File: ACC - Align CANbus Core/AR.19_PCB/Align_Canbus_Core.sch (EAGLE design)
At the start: 32 parts

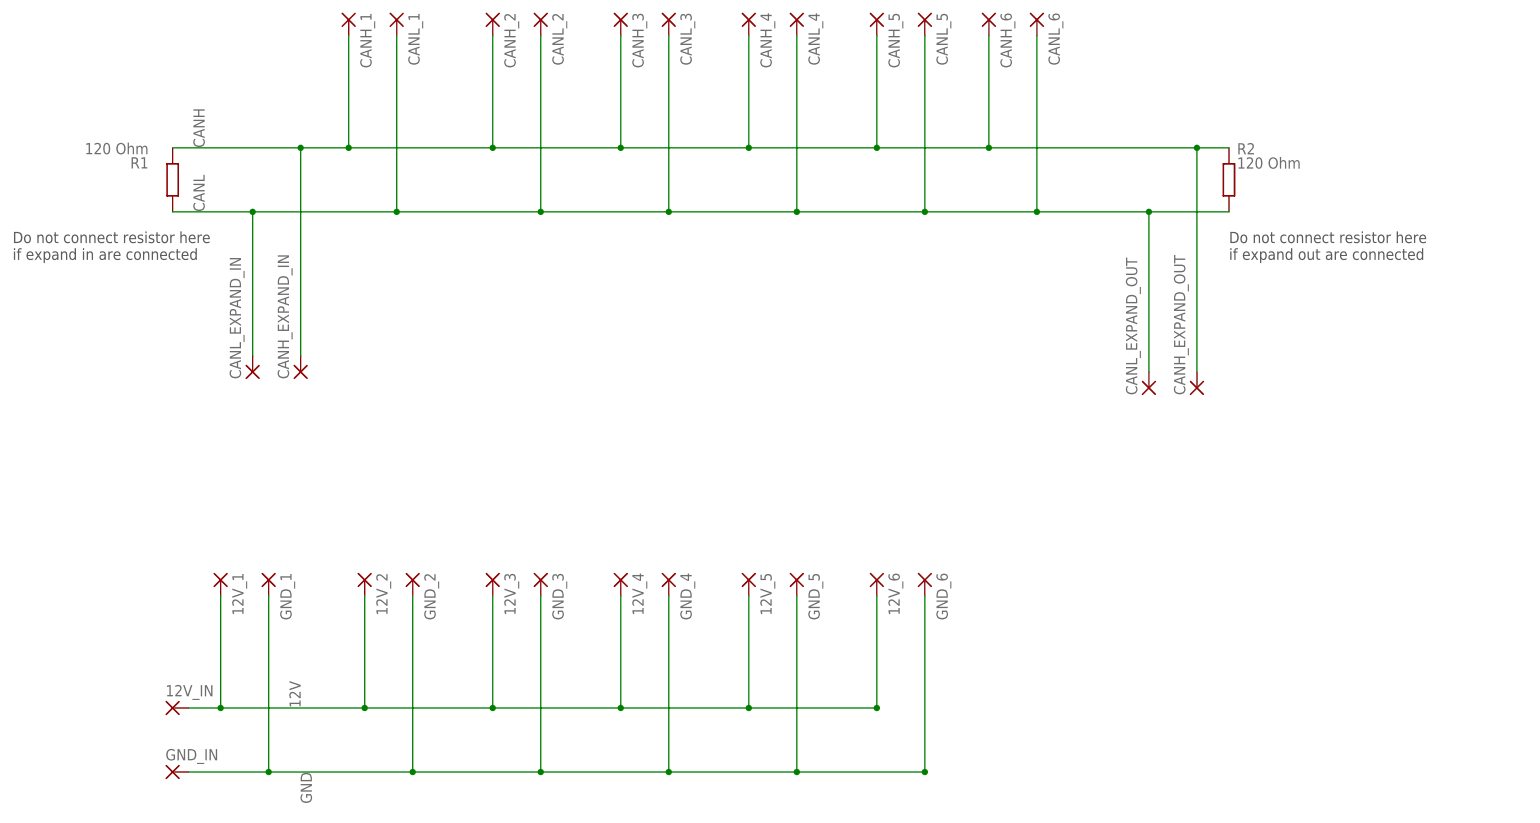
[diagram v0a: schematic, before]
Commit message: CANbus Core: Input and output expansion added
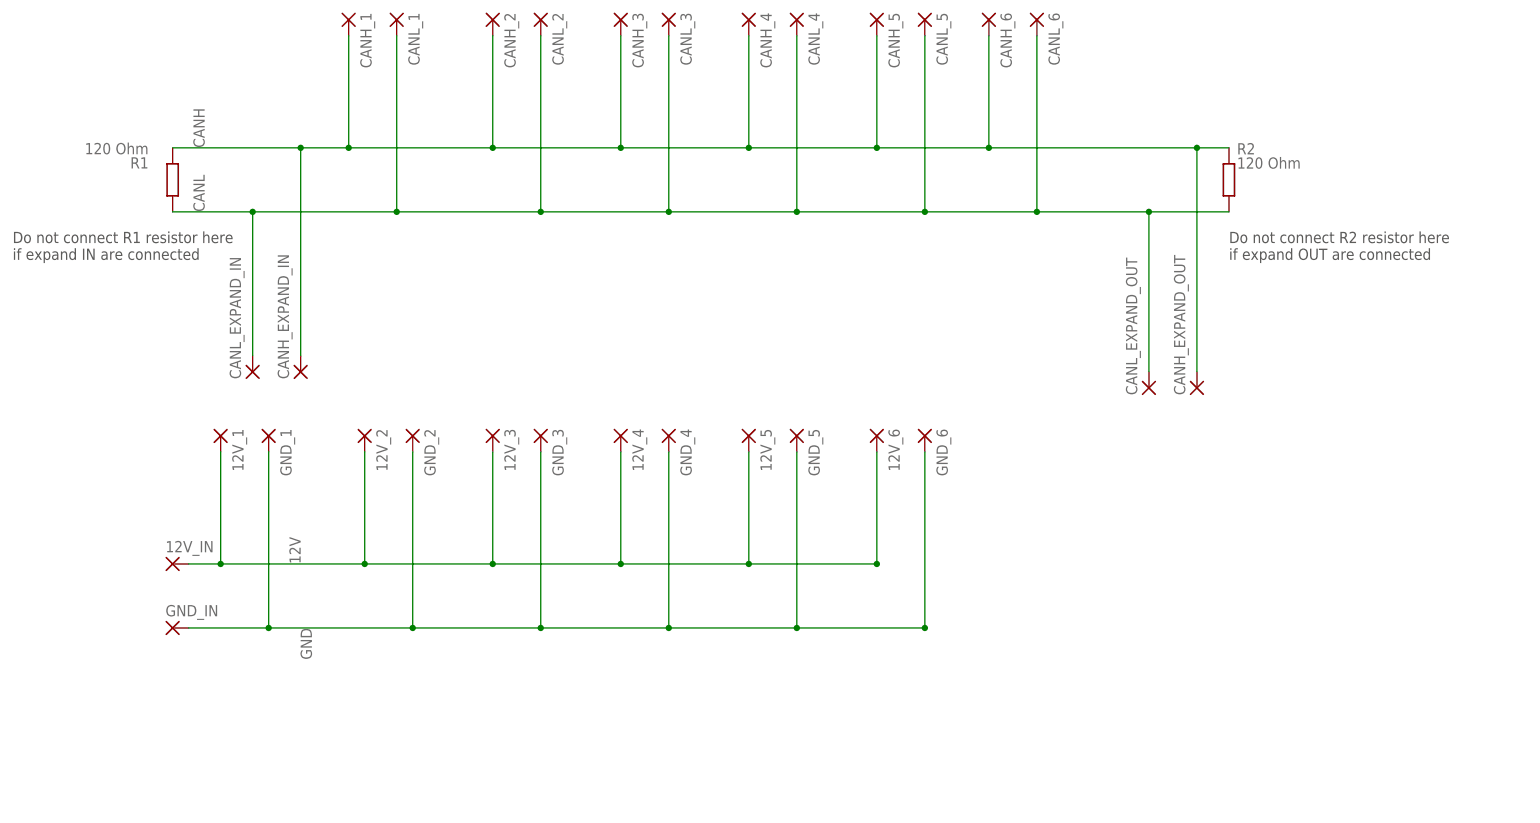
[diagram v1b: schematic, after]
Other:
- note added: "Do not connect R1 resistor here if expand IN are connected"
- note added: "Do not connect R2 resistor here if expand OUT are connected"
- note removed: "Do not connect resistor here if expand in are connected"
- note removed: "Do not connect resistor here if expand out are connected"
- moved on the sheet: 12V_1, 12V_2, 12V_3, 12V_4, 12V_5, 12V_6, 12V_IN, GND_1, GND_2, GND_3, GND_4, GND_5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
